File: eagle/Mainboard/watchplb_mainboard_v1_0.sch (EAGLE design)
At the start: 214 parts, among them IC2 BM70BLES1FC2-0B03AA, IC3 LM1117DTX-ADJ-12V, IC5 LM1117DTX-ADJ-10V, IC6 LM1117DTX-ADJ-3V3, J3 BNCPTH, Q1 8MHz / LFXTAL020423Reel, Q2 BC817-25SMD, Q3 DMN3023L-7, Q4 16MHz_LFXTAL051370Reel, Q5 CSD18534Q5A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

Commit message: Änderungen laut Besprechung mit Armin (soweit ich mich erinnern kann, ist schon ne woche her)
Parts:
- removed U$1: AX5031, Hick:AX5031
- removed U$3: LT1513, Hick:LT1513
- added IC1: LT1513, Hick:LT1513
- added IC4: AX5031, Hick:AX5031
- BAT_PACK_POS: value PTR1B2,54 -> PTR1B1,27; device testpad:PTR1B2,54 -> testpad:PTR1B1,27
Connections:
- net ANT_N: now also IC4.ANTN; no longer U$1.ANTN
- net ANT_P: now also IC4.ANTP; no longer U$1.ANTP
- net CHARGER_SS: now also IC1.S/S; no longer U$3.S/S
- net GND: now also IC1.GND, IC4.GND_PAD; no longer U$1.GND_PAD, U$3.GND
- net INT_POWER: now also IC4.VDD1, IC4.VDD2, IC4.VREG; no longer U$1.VDD1, U$1.VDD2, U$1.VREG
- net N$33: now also IC4.CLOCK16P; no longer U$1.CLOCK16P
- net N$34: now also IC4.CLOCK16N; no longer U$1.CLOCK16N
- net N$37: now also IC4.SYSCLK; no longer U$1.SYSCLK
- net N$61: now also IC1.VSW; no longer U$3.VSW
- net N$69: now also IC1.VIN; no longer U$3.VIN
- net N$72: now also IC1.VC; no longer U$3.VC
- net N$76: now also IC1.IFB; no longer U$3.IFB
- net N$77: now also IC1.VFB; no longer U$3.VFB
- net N$82: now also IC4.VDD_IO; no longer U$1.VDD_IO
- net SPI2_CLK: now also IC4.CLK; no longer U$1.CLK
- net SPI2_IRQ: now also IC4.IRQ; no longer U$1.IRQ
- net SPI2_MISO: now also IC4.MISO_SDO; no longer U$1.MISO_SDO
- net SPI2_MOSI: now also IC4.MOSI_SDI; no longer U$1.MOSI_SDI
- net SPI2_SEL_RFTX: now also IC4.SEL; no longer U$1.SEL
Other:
- note added: "Battery Protection"
- note added: "Linear Voltage Regulators"

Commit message: started BOM
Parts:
- C28, C31: value (none) -> 7.5pF
- C29, C30: value (none) -> 2.7pF
- C32, C33: value (none) -> 6pF
- C34, C35: value (none) -> 5.2pF
- C36, C37: value (none) -> NC
- L1, L4: value INDUCTOR-0805-3.3UH -> 39nH
- L2, L3: value INDUCTOR-0805-3.3UH -> 120nH
- L5, L6: value INDUCTOR-0805-3.3UH -> 27nH
- L7: value INDUCTOR-0805-3.3UH -> 0R

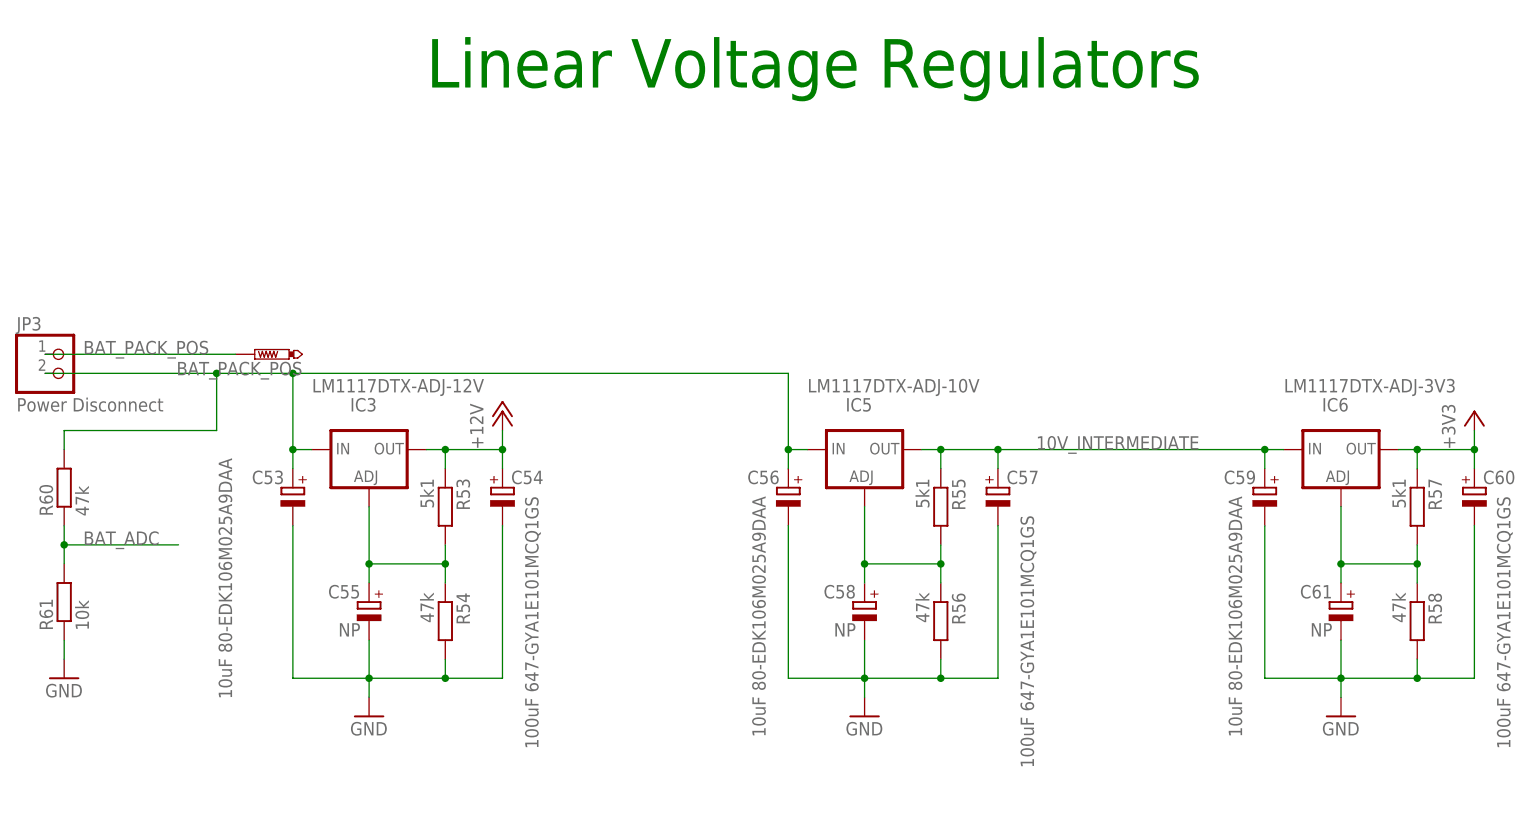
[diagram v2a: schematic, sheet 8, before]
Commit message: Noticed that I forgot to apply the Calculations for Linear Voltage Regulators to eagle, fixed this
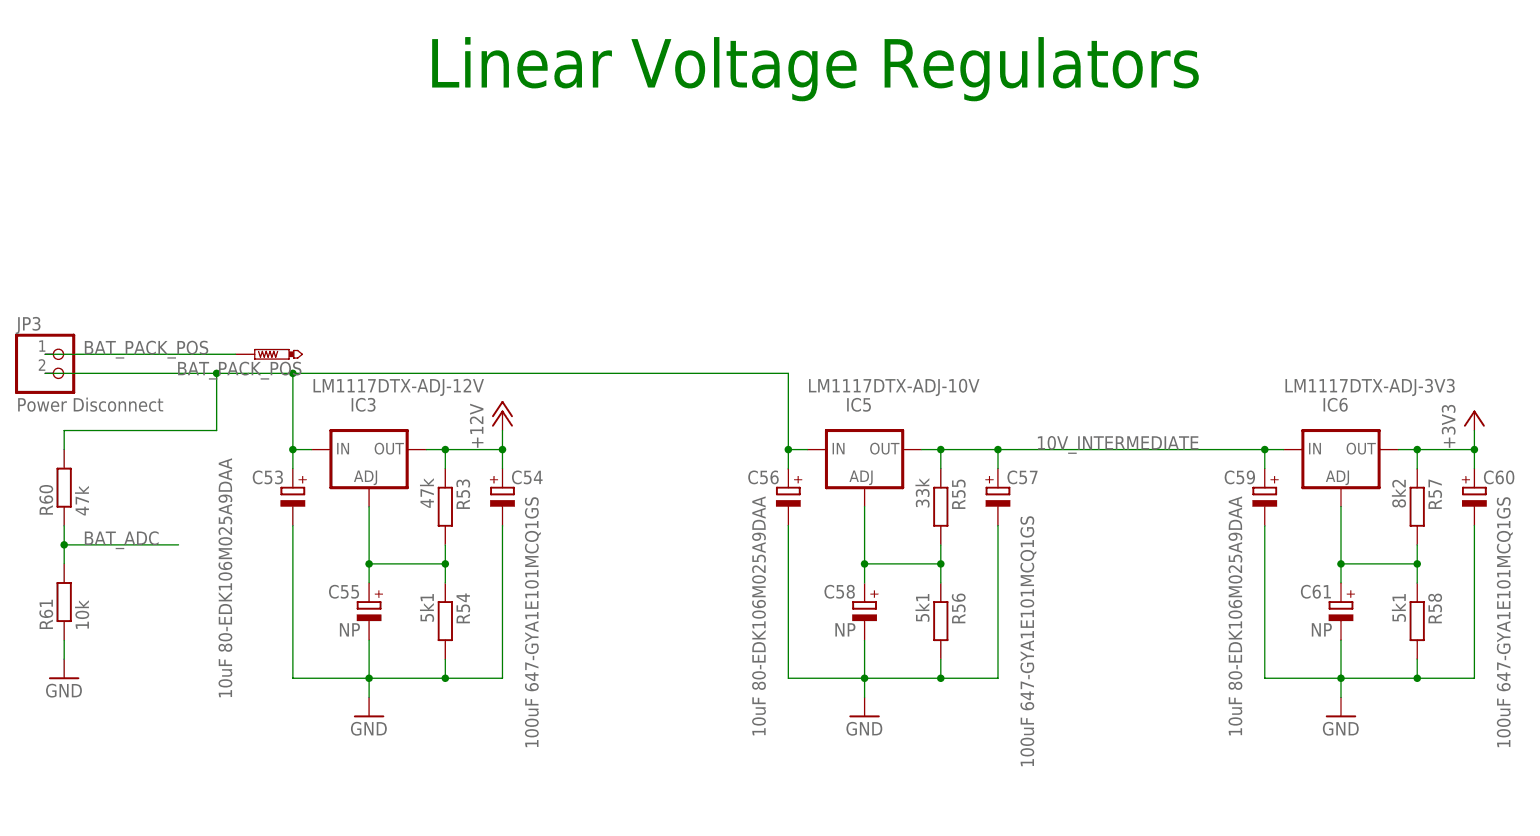
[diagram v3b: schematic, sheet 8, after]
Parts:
- R53: value 5k1 -> 47k
- R54, R56, R58: value 47k -> 5k1
- R55: value 5k1 -> 33k
- R57: value 5k1 -> 8k2
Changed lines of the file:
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@@
 <setting verticaltext="up"/>
 </settings>
-<grid distance="20" unitdist="mil" unit="mil" style="lines" multiple="1" display="yes" altdistance="0.01" altunitdist="inch" altunit="inch"/>
+<grid distance="0.1" unitdist="inch" unit="inch" style="lines" multiple="1" display="no" altdistance="0.01" altunitdist="inch" altunit="inch"/>
 <layers>
 <layer number="1" name="Top" color="4" fill="1" visible="no" active="no"/>
@@
 <part name="C53" library="rcl" deviceset="CPOL-EU" device="E" value="10uF  80-EDK106M025A9DAA  "/>
 <part name="C54" library="rcl" deviceset="CPOL-EU" device="E" value="100uF  647-GYA1E101MCQ1GS "/>
-<part name="R53" library="resistor" deviceset="R-EU_" device="M0805" value="5k1"/>
-<part name="R54" library="resistor" deviceset="R-EU_" device="M0805" value="47k"/>
+<part name="R53" library="resistor" deviceset="R-EU_" device="M0805" value="47k"/>
+<part name="R54" library="resistor" deviceset="R-EU_" device="M0805" value="5k1"/>
 <part name="P+2" library="supply1" deviceset="+12V" device=""/>
 <part name="C55" library="rcl" deviceset="CPOL-EU" device="E" value="NP"/>
@@
 <part name="C56" library="rcl" deviceset="CPOL-EU" device="E" value="10uF  80-EDK106M025A9DAA  "/>
 <part name="C57" library="rcl" deviceset="CPOL-EU" device="E" value="100uF  647-GYA1E101MCQ1GS "/>
-<part name="R55" library="resistor" deviceset="R-EU_" device="M0805" value="5k1"/>
-<part name="R56" library="resistor" deviceset="R-EU_" device="M0805" value="47k"/>
+<part name="R55" library="resistor" deviceset="R-EU_" device="M0805" value="33k"/>
+<part name="R56" library="resistor" deviceset="R-EU_" device="M0805" value="5k1"/>
 <part name="C58" library="rcl" deviceset="CPOL-EU" device="E" value="NP"/>
 <part name="IC6" library="lm1117" deviceset="LM1117DTX-ADJ" device="" value="LM1117DTX-ADJ-3V3"/>
 <part name="C59" library="rcl" deviceset="CPOL-EU" device="E" value="10uF  80-EDK106M025A9DAA  "/>
 <part name="C60" library="rcl" deviceset="CPOL-EU" device="E" value="100uF  647-GYA1E101MCQ1GS "/>
-<part name="R57" library="resistor" deviceset="R-EU_" device="M0805" value="5k1"/>
-<part name="R58" library="resistor" deviceset="R-EU_" device="M0805" value="47k"/>
+<part name="R57" library="resistor" deviceset="R-EU_" device="M0805" value="8k2"/>
+<part name="R58" library="resistor" deviceset="R-EU_" device="M0805" value="5k1"/>
 <part name="C61" library="rcl" deviceset="CPOL-EU" device="E" value="NP"/>
 <part name="GND36" library="supply1" deviceset="GND" device=""/>

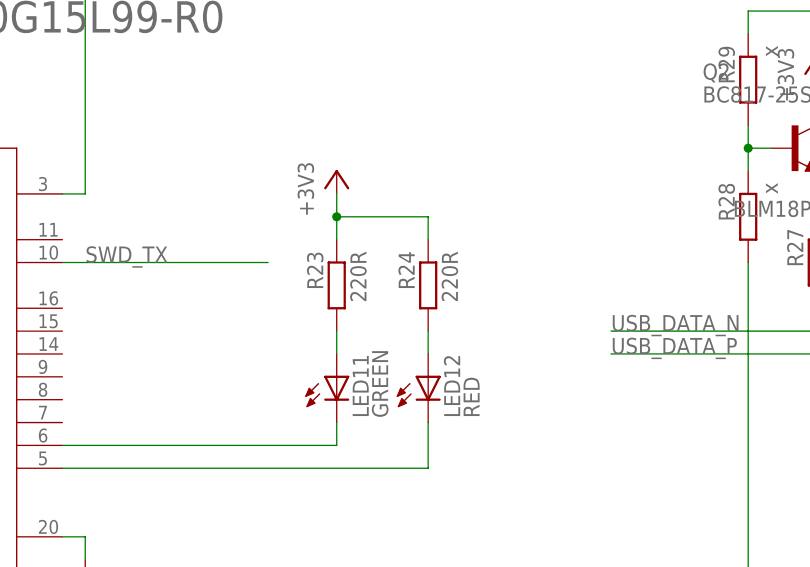
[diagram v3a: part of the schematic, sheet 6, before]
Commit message: small schematic changes
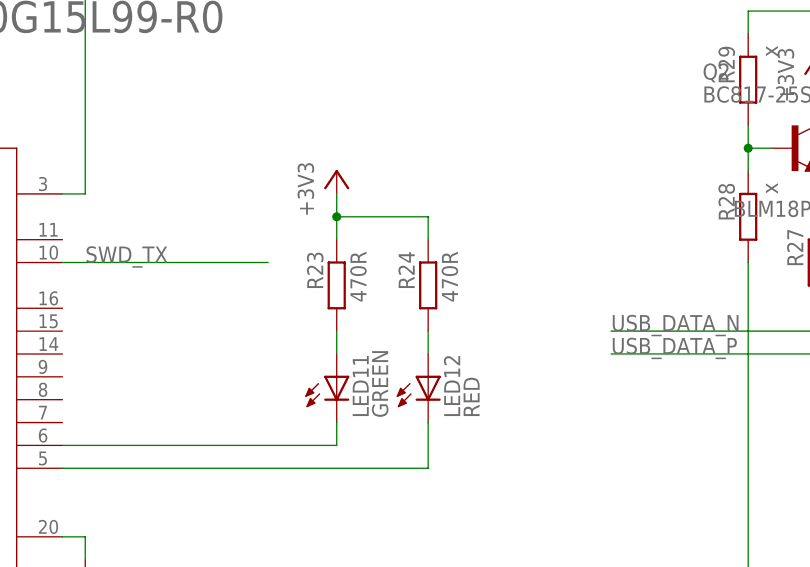
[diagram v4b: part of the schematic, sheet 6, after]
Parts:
- R23, R24: value 220R -> 470R
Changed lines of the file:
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@@
 <part name="+3V20" library="supply1" deviceset="+3V3" device=""/>
 <part name="LED11" library="adafruit" deviceset="LED" device="CHIP-LED0805" value="GREEN"/>
-<part name="R23" library="resistor" deviceset="R-EU_" device="M0805" value="220R"/>
-<part name="R24" library="resistor" deviceset="R-EU_" device="M0805" value="220R"/>
+<part name="R23" library="resistor" deviceset="R-EU_" device="M0805" value="470R"/>
+<part name="R24" library="resistor" deviceset="R-EU_" device="M0805" value="470R"/>
 <part name="LED12" library="adafruit" deviceset="LED" device="CHIP-LED0805" value="RED"/>
 <part name="+3V22" library="supply1" deviceset="+3V3" device=""/>

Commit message: Accumulated Changes over a few weeks
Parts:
- R49: value 10k -> 3k9
- R51: value 120k -> 155k
- R53: value 47k -> 5k1
- R54: value 5k1 -> 39k
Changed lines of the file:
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@@
 <part name="R48" library="resistor" deviceset="R-EU_" device="M0805" value="330k"/>
 <part name="C49" library="resistor" deviceset="C-EU" device="C0805K" value="100nF"/>
-<part name="R49" library="resistor" deviceset="R-EU_" device="M0805" value="10k"/>
+<part name="R49" library="resistor" deviceset="R-EU_" device="M0805" value="3k9"/>
 <part name="R50" library="resistor" deviceset="R-EU_" device="R2512" value="0.25R"/>
-<part name="R51" library="resistor" deviceset="R-EU_" device="M0805" value="120k"/>
+<part name="R51" library="resistor" deviceset="R-EU_" device="M0805" value="155k"/>
 <part name="R52" library="resistor" deviceset="R-EU_" device="M0805" value="12k4"/>
 <part name="C51" library="rcl" deviceset="CPOL-EU" device="E" value="22uF 80-EDK226M050A9GAA "/>
@@
 <part name="C53" library="rcl" deviceset="CPOL-EU" device="E" value="10uF  80-EDK106M025A9DAA  "/>
 <part name="C54" library="rcl" deviceset="CPOL-EU" device="E" value="100uF  647-GYA1E101MCQ1GS "/>
-<part name="R53" library="resistor" deviceset="R-EU_" device="M0805" value="47k"/>
-<part name="R54" library="resistor" deviceset="R-EU_" device="M0805" value="5k1"/>
+<part name="R53" library="resistor" deviceset="R-EU_" device="M0805" value="5k1"/>
+<part name="R54" library="resistor" deviceset="R-EU_" device="M0805" value="39k"/>
 <part name="P+2" library="supply1" deviceset="+12V" device=""/>
 <part name="C55" library="rcl" deviceset="CPOL-EU" device="E" value="NP"/>

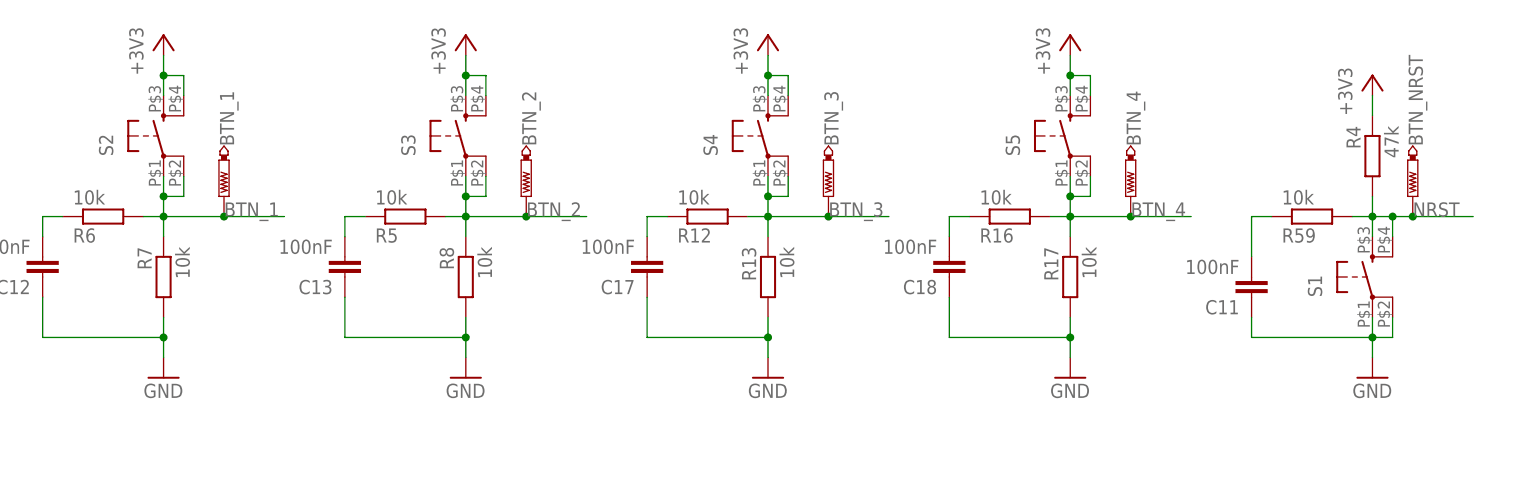
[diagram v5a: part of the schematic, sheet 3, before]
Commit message: einige kleine Änderungen: mcp111 ist smd massen verbinden taster footprint richtig orientierungspunkt U5 BQ ding richtungsmarkierung bei diode im Bat prot reset leitung bei pin verbinden LED rs auf 470R Charger SS pin mit pullup damits ohne firmware geht beschriftung am programmierheader verrutscht positiv beschriftung akkustecker usb 5v der unteren beiden trennen
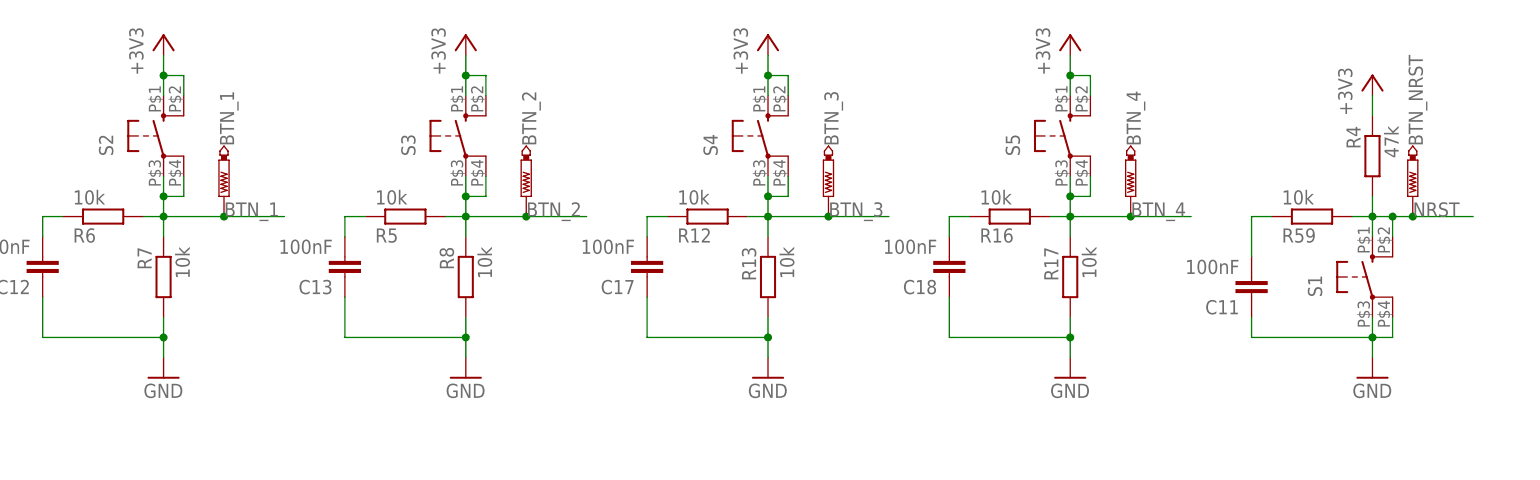
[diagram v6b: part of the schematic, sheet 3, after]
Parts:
- added R1, R2: 100k, resistor:R-EU_M0805
- U1: value MCP111-XXXXX/TO -> MCP111-XXXXX/TOSMD; device MCP111-XXXTO:MCP111-XXXXX/TO -> MCP111-XXXTO:MCP111-XXXXX/TOSMD
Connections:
- removed net +5V: FB1.2, J1.VBUS, R29.1, U3.VDD, U4.VCC
- new net N$41: J1.VBUS, U3.VDD
- new net N$44: FB1.2, R29.1, U4.VCC
- net +3V3: now also R2.2, S2.SL1, S2.SL2, S3.SL1, S3.SL2, S4.SL1, S4.SL2, S5.SL1, S5.SL2; no longer S2.S, S2.S1, S3.S, S3.S1, S4.S, S4.S1, S5.S, S5.S1
- net BTN_1: now also S2.SR1, S2.SR2; no longer S2.P, S2.P1
- net BTN_2: now also S3.SR1, S3.SR2; no longer S3.P, S3.P1
- net BTN_3: now also S4.SR1, S4.SR2; no longer S4.P, S4.P1
- net BTN_4: now also S5.SR1, S5.SR2; no longer S5.P, S5.P1
- net CHARGER_CH_PRECH: now also R1.1
- net CHARGER_SS: now also R2.1
- net GND: now also R1.2, S1.SR1, S1.SR2; no longer S1.P, S1.P1
- net NRST: now also S1.SL1, S1.SL2; no longer S1.S, S1.S1
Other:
- note added: "bnc.cable mouser nr 601-606BBP is required for connection to antenna"
- note added: "caps for crystal integrated in chip"
- note added: "with USB integrated in STM32"
- note added: "with USB-to-UART Chip"
- note removed: "caps for crysta integrated in chip"
- note removed: "kabel mouser nr 601-606BBP wird ebenfalls benötigt"
- note removed: "mit USB des STM"
- note removed: "mit USB-to-UART Chip"
